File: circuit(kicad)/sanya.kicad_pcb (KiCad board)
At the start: 2 copper layers, 33 x 28 mm, 10 parts, among them J1 Oled, J2 Micro_SD_Card, J3 AVR-ISP-6, SW1 Up, SW2 Down, SW3 Set, SW4 SW_DPDT_x2, U1 ATmega328P-A

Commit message: sshnk1
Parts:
- removed J3: AVR-ISP-6, Connector_IDC:IDC-Header_2x03_P2.54mm_Vertical
- moved U1 39.2 mm to (158.7, 59.8)
- moved SW3 35.7 mm to (169.6, 63.1)
- moved J1 32.9 mm to (154.9, 50.7), turned to 0 degrees
- moved SW4 31.4 mm to (164.0, 52.0)
- moved BT1 28.6 mm to (149.7, 63.0)
- moved SW1 27.9 mm to (169.6, 55.0)
- moved SW2 26.2 mm to (169.6, 71.3)
- moved R1 23.3 mm to (151.0, 58.8)
- moved J2 4.10 mm to (155.0, 70.0), turned to -90 degrees
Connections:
- BT1 pad 1: Net-(BT1-+) -> unconnected-(BT1-+-Pad1)
- BT1 pad 2: Earth -> Net-(BT1--)
- SW4 pad 1: Net-(BT1-+) -> Net-(BT1--)
- SW4 pad 2: VCC -> Earth
- SW4 pad 3: unconnected-(SW4A-C-Pad3) -> /RST
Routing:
- net Earth: track 0.00 -> 114.3 mm, vias 0 -> 2
- net VCC: track 0.00 -> 50.6 mm
- net /RST: track 0.00 -> 24.5 mm, vias 0 -> 3
- net /PD6: track 0.00 -> 18.6 mm, vias 0 -> 2
- net /PD5: track 0.00 -> 18.0 mm, vias 0 -> 2
- net /PD4: track 0.00 -> 17.7 mm, vias 0 -> 2
- net Net-(BT1--): track 0.00 -> 16.0 mm
- net /SCK: track 0.00 -> 15.3 mm, vias 0 -> 2
- net /MISO: track 0.00 -> 14.3 mm
- net /MOSI: track 0.00 -> 8.94 mm
- net /SCL: track 0.00 -> 7.96 mm
- net /PB2: track 0.00 -> 6.95 mm
- net /SDA: track 0.00 -> 5.42 mm
- net unconnected-(BT1-+-Pad1): track 0.00 -> 0.10 mm, vias 0 -> 2
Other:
- board size 33 x 28 mm -> 33.6 x 26.3 mm

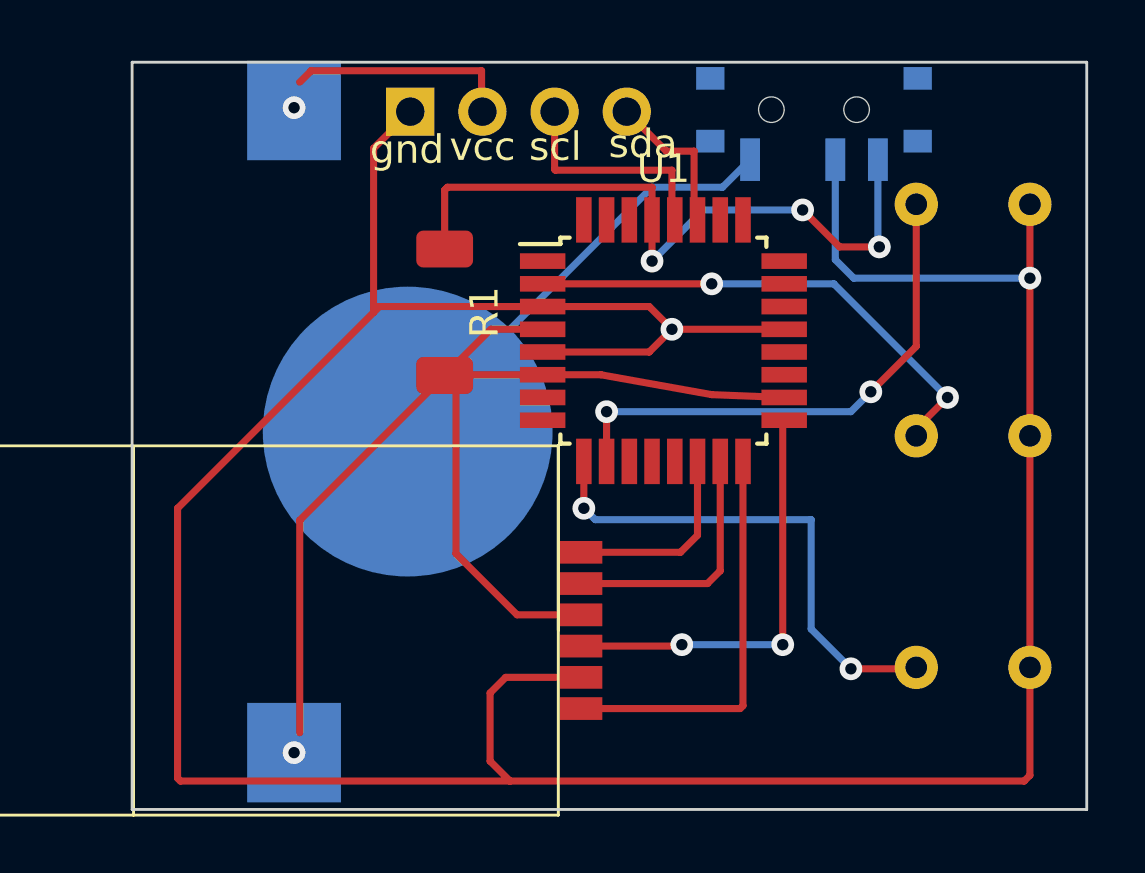
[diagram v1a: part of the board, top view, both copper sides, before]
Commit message: Изменил размер дорожек и переходных отверстий
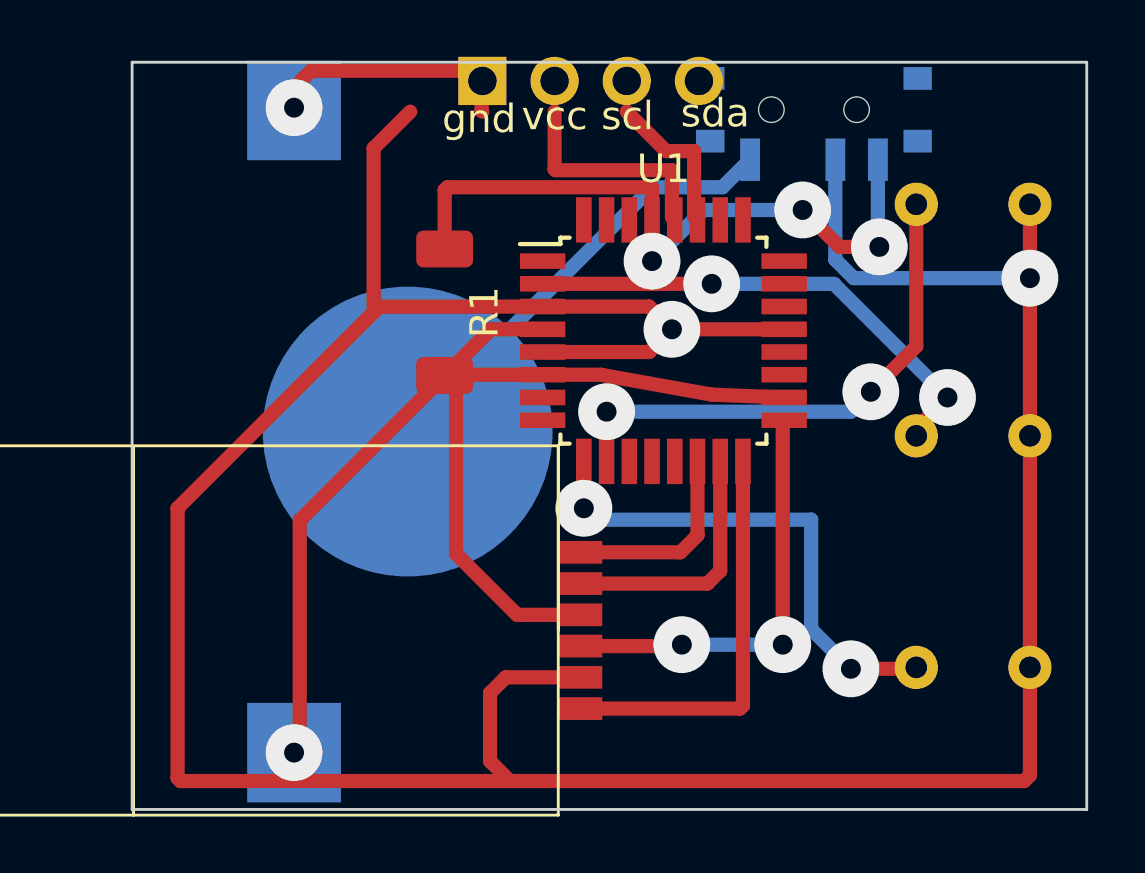
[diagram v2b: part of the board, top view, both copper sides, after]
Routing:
- net VCC: track 50.6 -> 42.6 mm
- net Earth: track 114.3 -> 122.3 mm

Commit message: Подкорректировал посадочные места, провел дорожки автотрассировщиком (еще не финальный вариант)
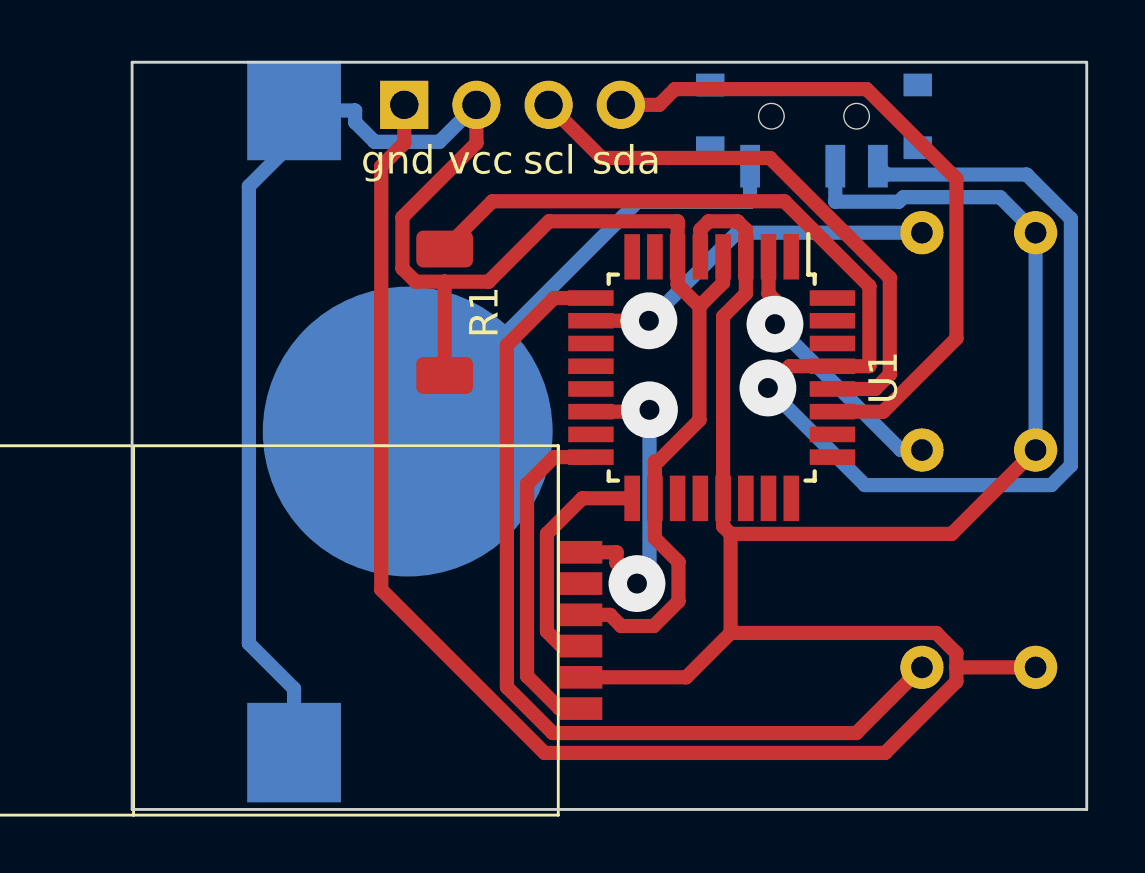
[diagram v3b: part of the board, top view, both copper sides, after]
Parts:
- moved J1 2.88 mm to (152.1, 51.5)
- moved U1 2.14 mm to (160.4, 61.1), turned to -90 degrees
- moved SW1 1.02 mm to (169.8, 56.0)
- moved SW3 0.54 mm to (169.8, 63.6)
- moved SW4 0.23 mm to (164.0, 52.2)
- moved SW2 0.20 mm to (169.8, 71.3)
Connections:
- BT1 pad 1: unconnected-(BT1-+-Pad1) -> VCC
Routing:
- net VCC: track 42.6 -> 73.7 mm
- net /RST: track 24.5 -> 52.2 mm, vias 3 -> 1
- net /SDA: track 5.42 -> 24.4 mm
- net Earth: track 122.3 -> 104.9 mm, vias 2 -> 0
- net /PD5: track 18.0 -> 31.9 mm, vias 2 -> 0
- net /SCL: track 7.96 -> 20.2 mm
- net /MOSI: track 8.94 -> 0.00 mm
- net /PD4: track 17.7 -> 9.47 mm, vias 2 -> 1
- net /SCK: track 15.3 -> 8.37 mm, vias 2 -> 0
- net /PD6: track 18.6 -> 12.9 mm, vias 2 -> 1
- net /PB2: track 6.95 -> 11.0 mm, vias 0 -> 2
- net /MISO: track 14.3 -> 11.8 mm
- net Net-(BT1--): track 16.0 -> 16.7 mm
- net unconnected-(BT1-+-Pad1): track 0.10 -> 0.00 mm, vias 2 -> 0

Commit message: Дорожки вроде как протрассированы финально. Осталось увеличить между ними расстояние и некоторые переходные отверстия отодвинуть (смотри по 3D-чертежу, там видно, что некоторые компоненты закрывают переходные отверстия)
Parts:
- moved BT1 7.17 mm to (154.3, 68.5)
- moved SW3 7.17 mm to (174.4, 69.2)
- moved J1 7.17 mm to (156.7, 57.0)
- moved J2 7.17 mm to (159.6, 75.5)
- moved SW1 7.17 mm to (174.4, 61.5)
- moved SW2 7.17 mm to (174.4, 76.8)
- moved SW4 7.17 mm to (168.6, 57.7)
- moved U1 7.17 mm to (165.0, 66.6), turned to 0 degrees
- moved R1 5.05 mm to (152.6, 63.6), turned to 180 degrees
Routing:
- net Earth: track 104.9 -> 74.9 mm, vias 0 -> 3
- net /RST: track 52.2 -> 23.4 mm
- net /SDA: track 24.4 -> 39.6 mm, vias 0 -> 1
- net /SCK: track 8.37 -> 20.1 mm
- net VCC: track 73.7 -> 84.6 mm, vias 0 -> 1
- net /MOSI: track 0.00 -> 8.80 mm
- net /PD4: track 9.47 -> 17.9 mm
- net /SCL: track 20.2 -> 11.8 mm, vias 0 -> 1
- net /PB2: track 11.0 -> 7.35 mm, vias 2 -> 0
- net /PD5: track 31.9 -> 28.5 mm, vias 0 -> 1
- net /PD6: track 12.9 -> 14.2 mm
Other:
- board size 33.6 x 26.3 mm -> 34.4 x 26.9 mm

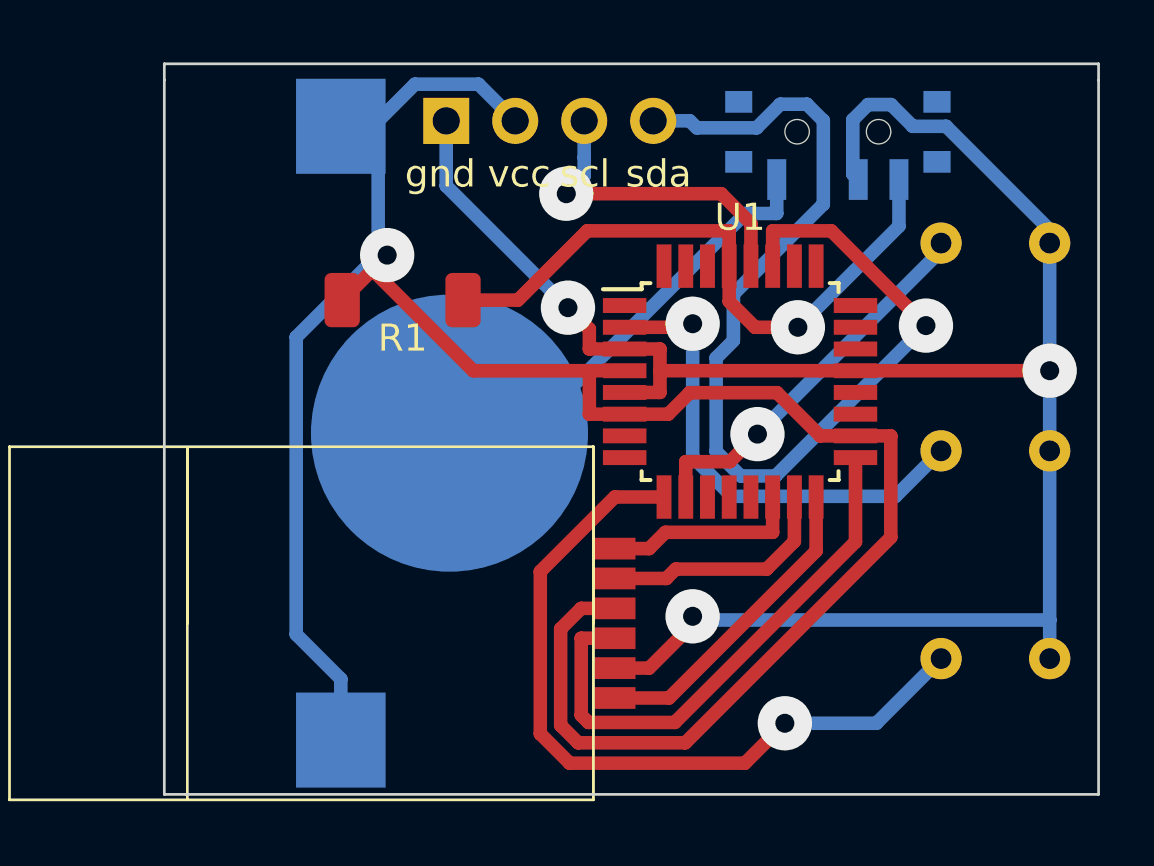
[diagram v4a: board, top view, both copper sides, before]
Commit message: Трассировка завершена. Остались финальные штрихи: подровнять всё, добавить медную окантовку
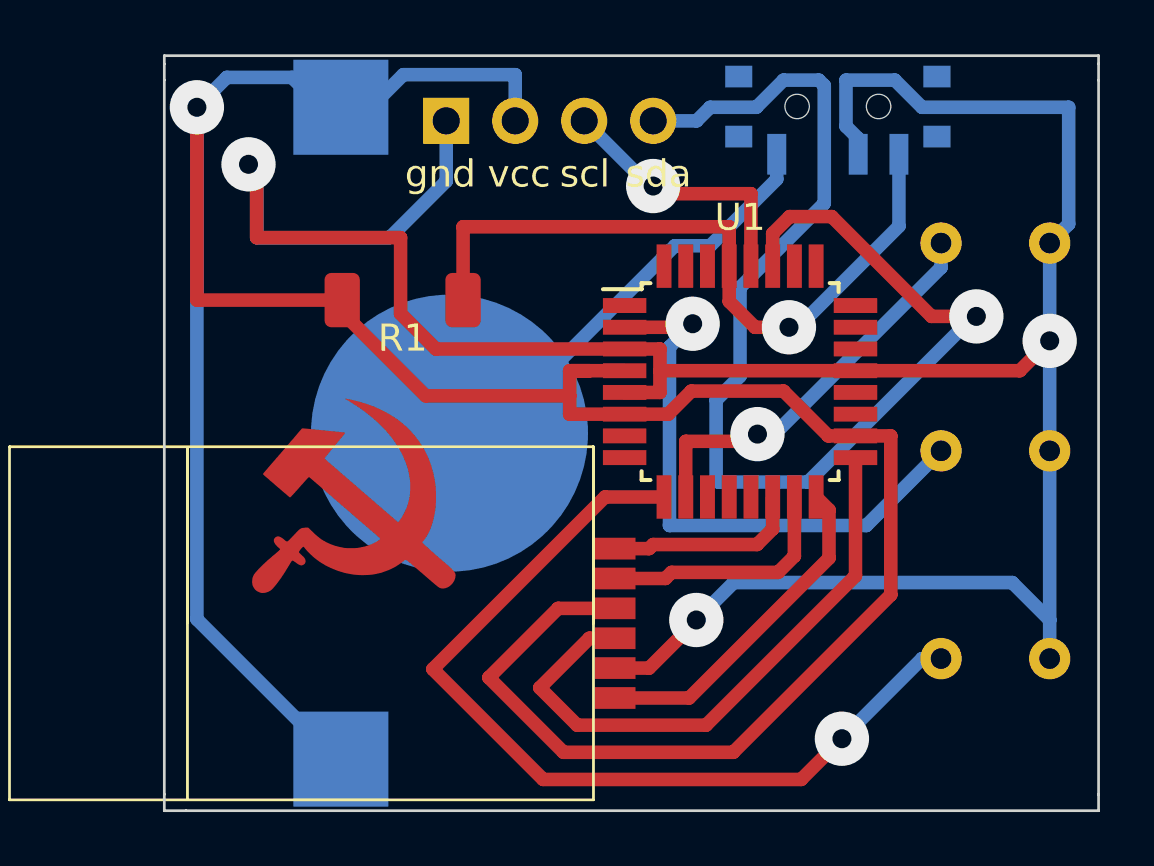
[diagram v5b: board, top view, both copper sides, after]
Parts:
- added G***: LOGO, posad, F.Cu at (150.8, 70.8)
- moved SW4 0.93 mm to (168.6, 56.8)
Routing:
- net VCC: track 84.6 -> 111.6 mm
- net Earth: track 74.9 -> 101.6 mm
- net /SDA: track 39.6 -> 45.8 mm
- net /PD5: track 28.5 -> 33.4 mm
- net /PD4: track 17.9 -> 21.5 mm
- net /RST: track 23.4 -> 26.1 mm
- net /SCK: track 20.1 -> 22.4 mm
- net /SCL: track 11.8 -> 9.92 mm
- net /MISO: track 11.6 -> 12.5 mm
- net /PD6: track 14.2 -> 15.0 mm
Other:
- board size 34.4 x 26.9 mm -> 34.4 x 27.8 mm
